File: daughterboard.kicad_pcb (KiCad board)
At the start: 4 copper layers, 70 x 90 mm, 62 parts, among them J1 USB_OTG, J10 J, J11 J, J12 J, J13 J, J14 J, J15 J, J16 J, J17 J, J2 MotorA, J24 J, J25 J, J26 J, J27 J, J28 J, J29 J, J3 MotorB, J30 J, J31 J, J32 J, J33 QTR-8A, J34 J, J35 J, J4 BARREL_JACK, J5 Debug, J6 J, J7 J, P1 CONN_01X02, P2 CONN_01X02, U1 LD1117S33CTR, U2 TB6612FNG, U3 EFM32G230F128, Y1 Crystal

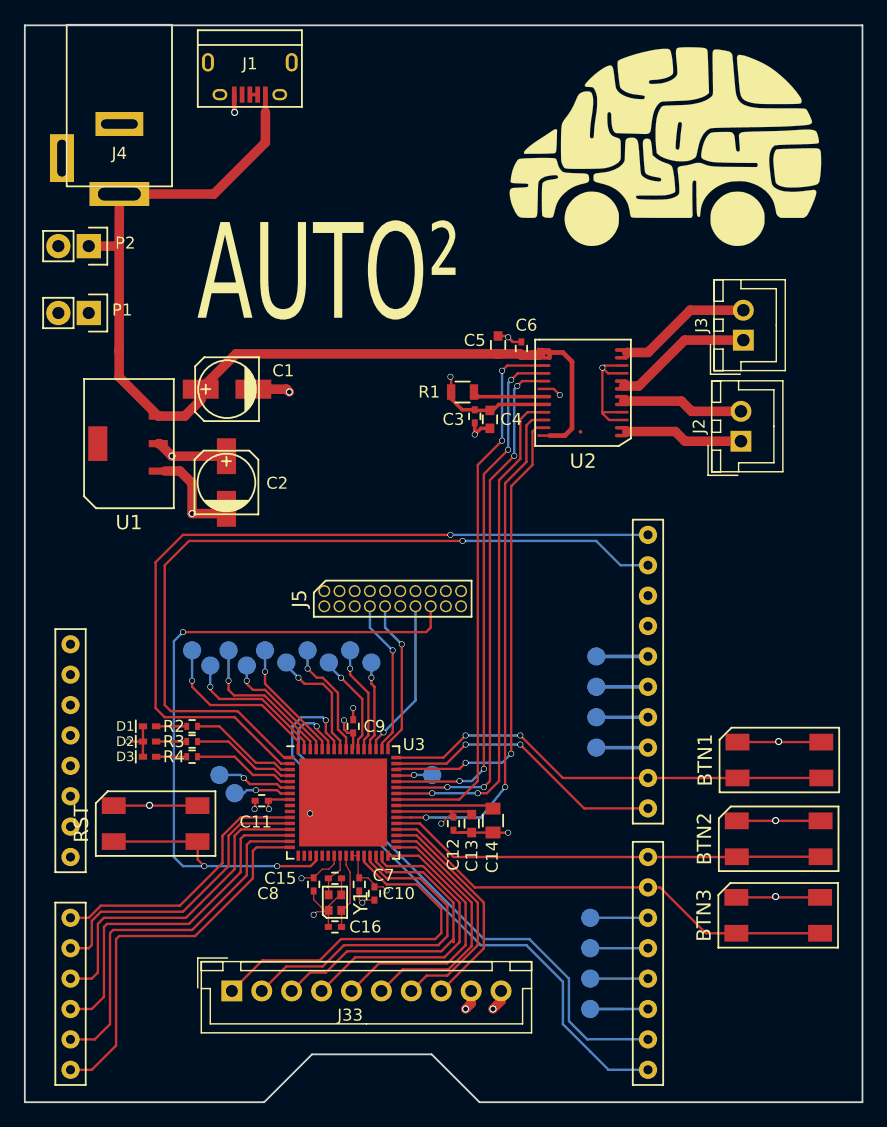
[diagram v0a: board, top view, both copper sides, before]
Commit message: Change via size
Seems to be a problem with thermal relief on the vias
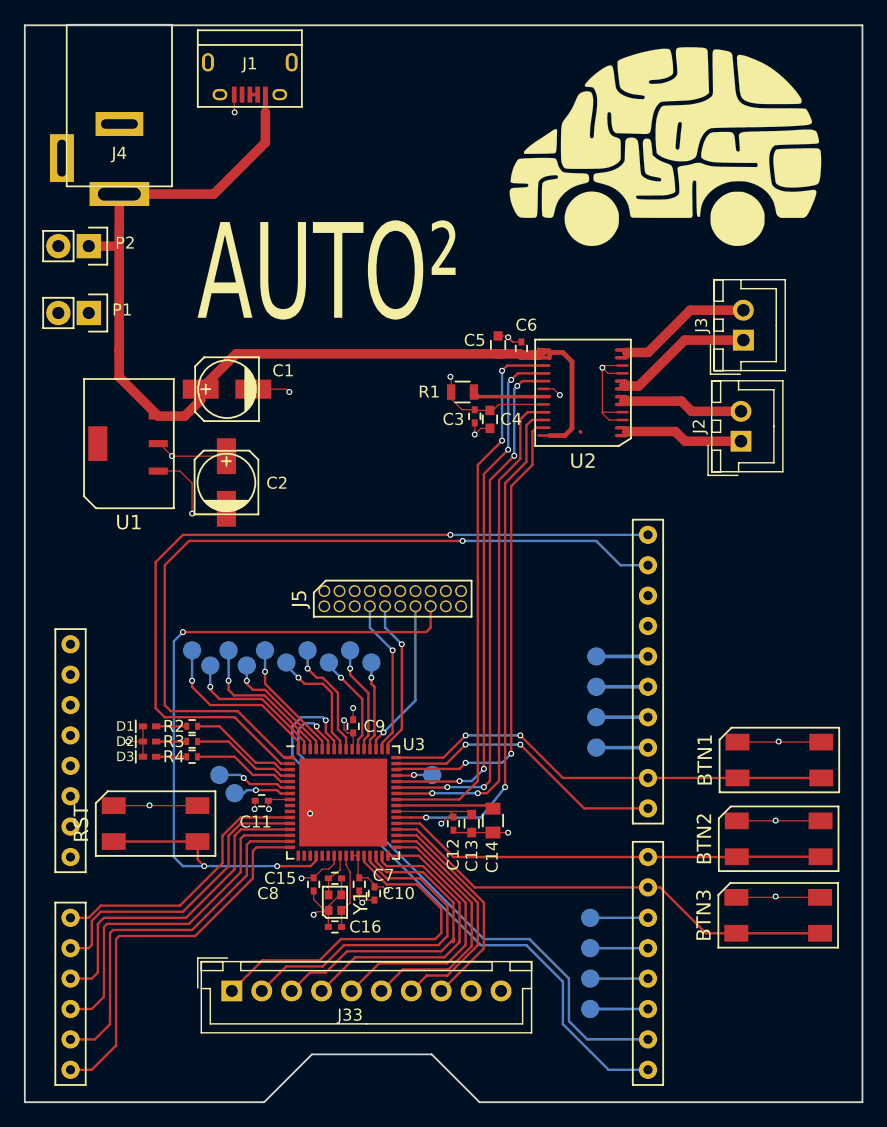
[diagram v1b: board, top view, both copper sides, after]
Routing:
- net +3V3: track 63.8 -> 61.2 mm, vias 11 -> 10
- net GND: track 90.4 -> 89.4 mm, vias 16 -> 15
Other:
- rule pad_to_mask_clearance: 0.2 -> 0.05

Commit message: Add names to Silkscreen
Also updated gerbers with the new silk screen
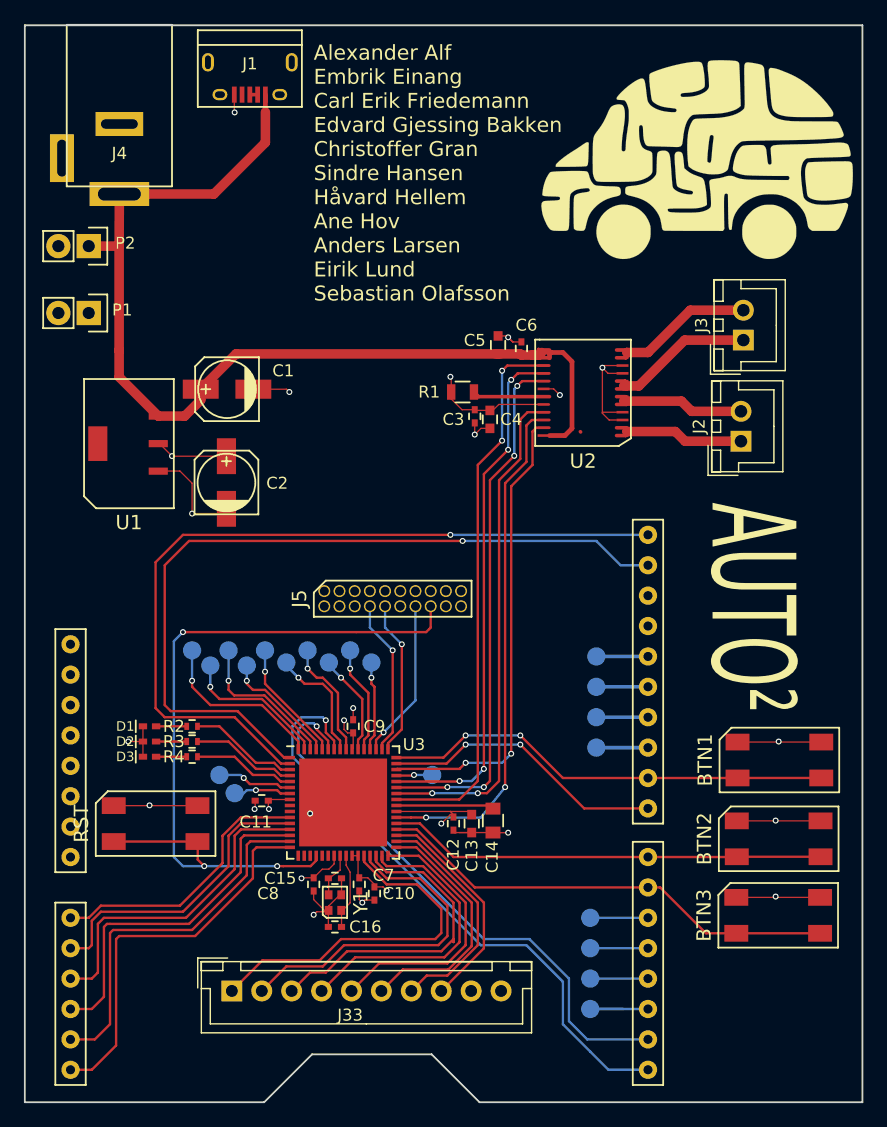
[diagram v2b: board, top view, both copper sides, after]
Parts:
- moved G*** 2.86 mm to (120.7, 69.1)
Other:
- board text added: "Alexander Alf Embrik Einang Carl Erik Friedemann Edvard Gjessing Bakken Christoffer Gran Sindre Hansen Håvard Hellem Ane Hov Anders Larsen Eirik Lund Sebastian Olafsson"
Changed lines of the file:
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@@
     (area 63.924999 56.405 143.973 148.075001)
     (thickness 1.6)
-    (drawings 9)
+    (drawings 10)
     (tracks 677)
     (zones 0)
@@
   )
   (module lib_fp:logo (layer F.Cu)
-    (at 118 68)
+    (at 120.65 69.088)
     (fp_text reference G*** (at 0 0) (layer F.SilkS) hide
       (effects (font (thickness 0.3)))
@@
       (net 1 +5V))
   )
-  (gr_text AUTO² (at 89.408 78.74) (layer F.SilkS)
-    (effects (font (size 8 5) (thickness 1)))
+  (gr_text "Alexander Alf\nEmbrik Einang\nCarl Erik Friedemann\nEdvard Gjessing Bakken\nChristoffer Gran\nSindre Hansen\nHåvard Hellem\nAne Hov\nAnders Larsen\nEirik Lund \nSebastian Olafsson" (at 88.138 70.358) (layer F.SilkS)
+    (effects (font (size 1.25 1.25) (thickness 0.3)) (justify left))
+  )
+  (gr_text AUTO² (at 124.714 106.68 270) (layer F.SilkS)
+    (effects (font (size 7 4) (thickness 1)))
   )
   (gr_line (start 102 148) (end 134 148) (angle 90) (layer Edge.Cuts) (width 0.15))
